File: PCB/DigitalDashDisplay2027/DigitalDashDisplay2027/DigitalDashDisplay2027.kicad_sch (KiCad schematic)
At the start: 13 parts, among them IC1 LMR51430YDDCR, J1 Adafruit CAN Pal, J2 53375-0810, U1 Teensy4.0

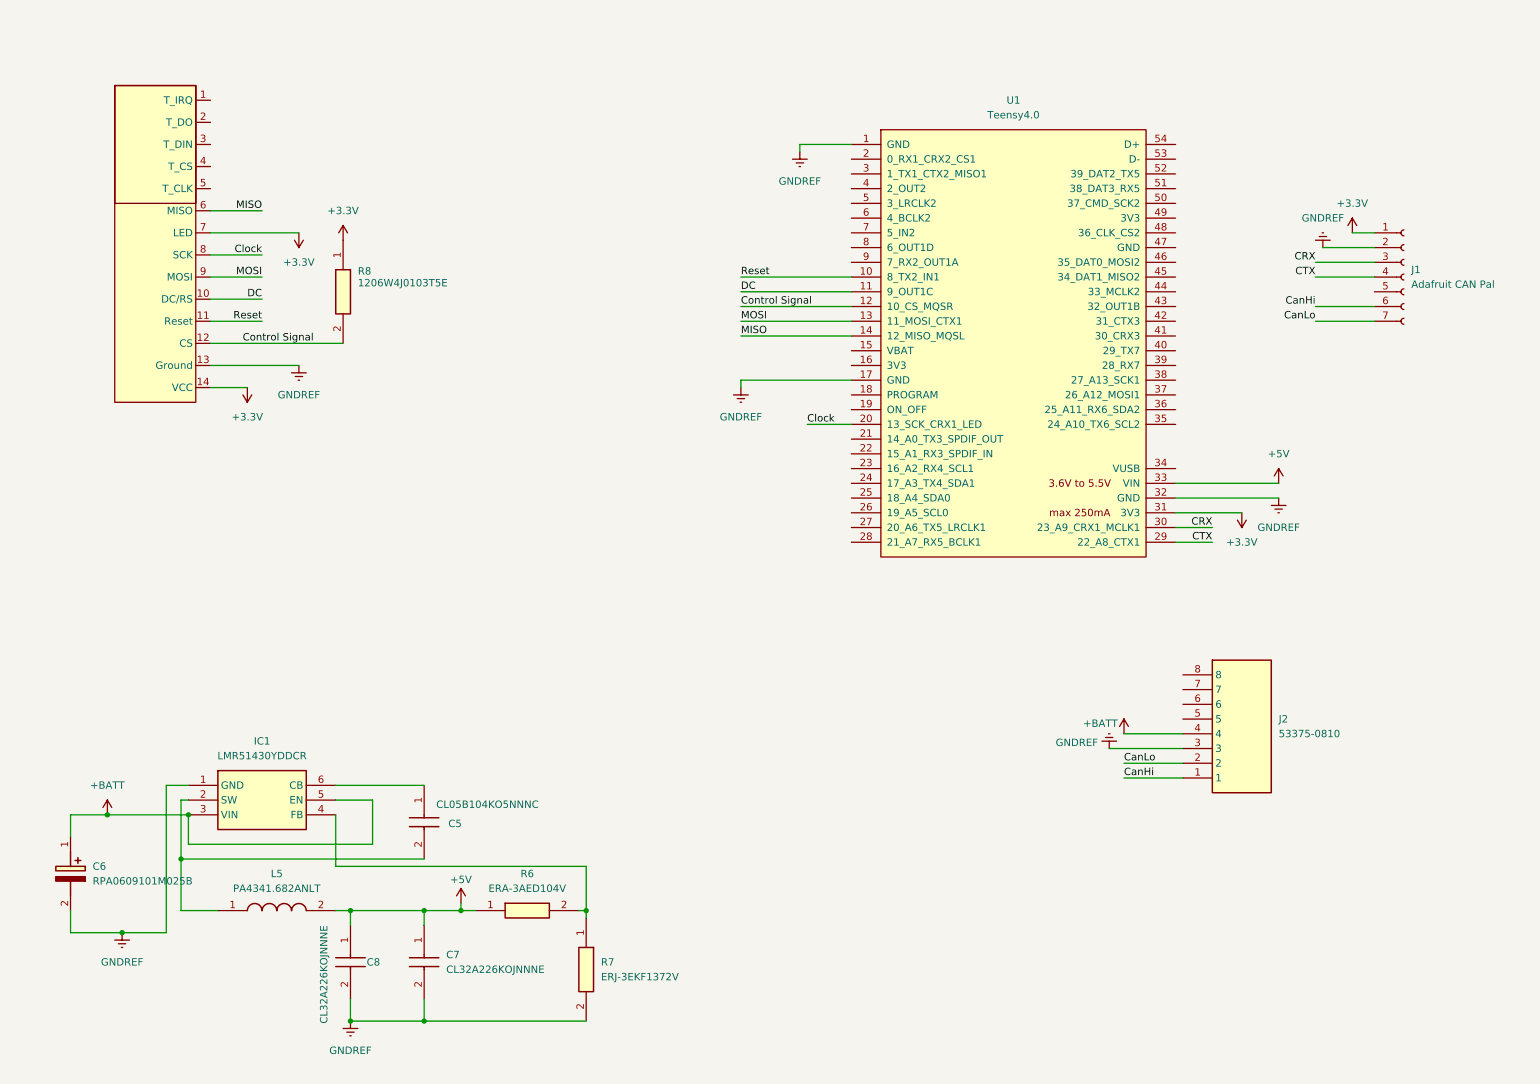
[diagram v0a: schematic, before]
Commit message: Began restructuring dash PCB, migrated footprints & symbols to the central library
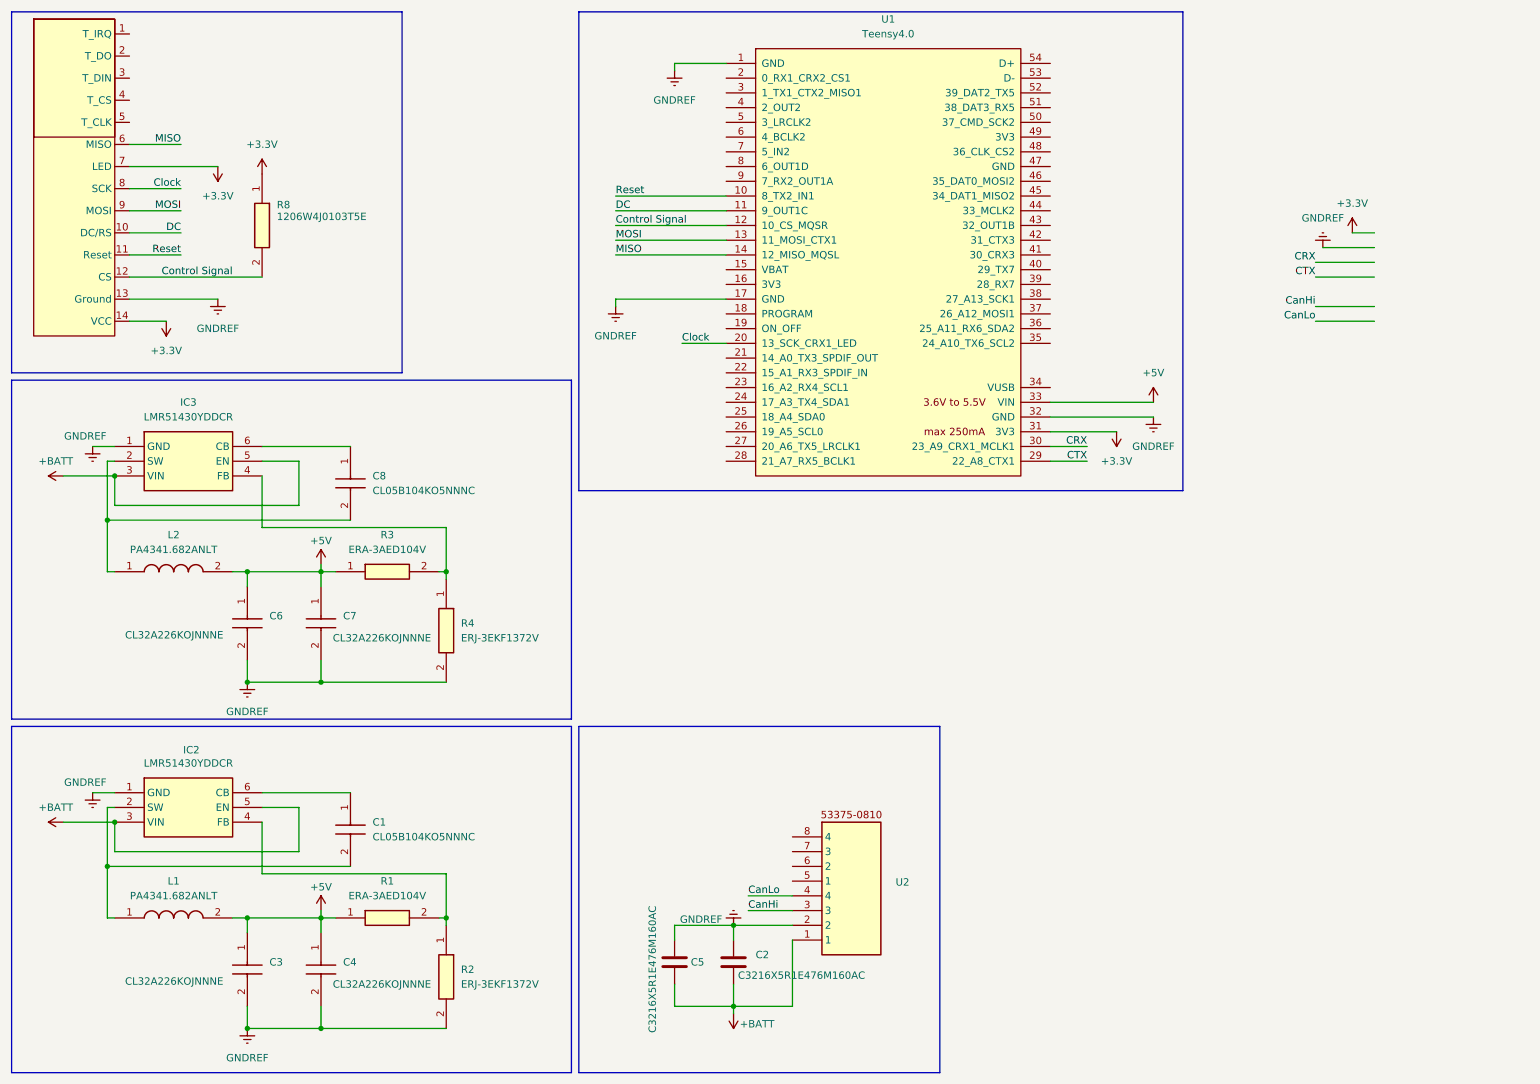
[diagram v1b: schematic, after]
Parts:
- removed C5: CL05B104KO5NNNC, buck_footprints:CAPC1005X55N, symbol CL05B104KO5NNNC:CL05B104KO5NNNC
- removed C6: RPA0609101M025B, buck_footprints:CAPPRD250W55D630H1050, symbol RPA0609101M025B:RPA0609101M025B
- removed C7, C8: CL32A226KOJNNNE, buck_footprints:CAPC3225X270N, symbol CL32A226KOJNNNE:CL32A226KOJNNNE
- removed IC1: LMR51430YDDCR, buck_footprints:SOT95P280X110-6N, symbol LMR51430YDDCR:LMR51430YDDCR
- removed J1: Adafruit CAN Pal, CFR 2025 Digital Dash Lib:1X07_ROUND_70, symbol Connector:Conn_01x07_Socket
- removed J2: 53375-0810, 533750810, symbol SamacSys_Parts:53375-0810
- removed L5: PA4341.682ANLT, buck_footprints:INDPM7166X300N, symbol PA4341_682ANLT:PA4341.682ANLT
- removed R6: ERA-3AED104V, buck_footprints:ERA3AEB101V, symbol ERA-3AED104V:ERA-3AED104V
- removed R7: ERJ-3EKF1372V, buck_footprints:RESC1608X55N, symbol ERJ-3EKF1372V:ERJ-3EKF1372V
- added C1, C8: CL05B104KO5NNNC, CAPC1005X55N, symbol CFR Library:CL05B104KO5NNNC
- added C2, C5: C3216X5R1E476M160AC, Capacitor_SMD:C_1206_3216Metric_Pad1.33x1.80mm_HandSolder, symbol Device:C
- added C3, C4, C6, C7: CL32A226KOJNNNE, CAPC3225X270N, symbol CFR Library:CL32A226KOJNNNE
- added IC2, IC3: LMR51430YDDCR, SOT95P280X110-6N, symbol CFR Library:LMR51430YDDCR
- added L1, L2: PA4341.682ANLT, INDPM7166X300N, symbol CFR Library:PA4341.682ANLT
- added R1, R3: ERA-3AED104V, ERA3AEB101V, symbol CFR Library:ERA-3AED104V
- added R2, R4: ERJ-3EKF1372V, RESC1608X55N, symbol CFR Library:ERJ-3EKF1372V
- added U2: (no value), CFR-Footprint-Library:CONN08_533750810_MOL, symbol CFR Library:53375-0810
- ILI1: value ~ -> (none)
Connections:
- net +5V: now also C3.1, C4.1, C6.1, C7.1, L1.2, L2.2, R1.1, R3.1
- net +BATT: now also C2.2, C5.2, IC2.3 (VIN), IC2.5 (EN), IC3.3 (VIN), IC3.5 (EN), U2.1
- net CanHi: now also U2.3
- net CanLo: now also U2.4
- net GNDREF: now also C2.1, C3.2, C4.2, C5.1, C6.2, C7.2, IC2.1 (GND), IC3.1 (GND), R2.2, R4.2, U2.2
- new net: C8.2, IC3.2 (SW), L2.1
- new net: C1.2, IC2.2 (SW), L1.1
- new net: IC2.4 (FB), R1.2, R2.1
- new net: IC3.4 (FB), R3.2, R4.1
- new net: C1.1, IC2.6 (CB)
- new net: C8.1, IC3.6 (CB)
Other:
- moved on the sheet: R8, U1

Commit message: Began redesigning dashboard, changed multi-power rail to single power rail, rerouted buck converter
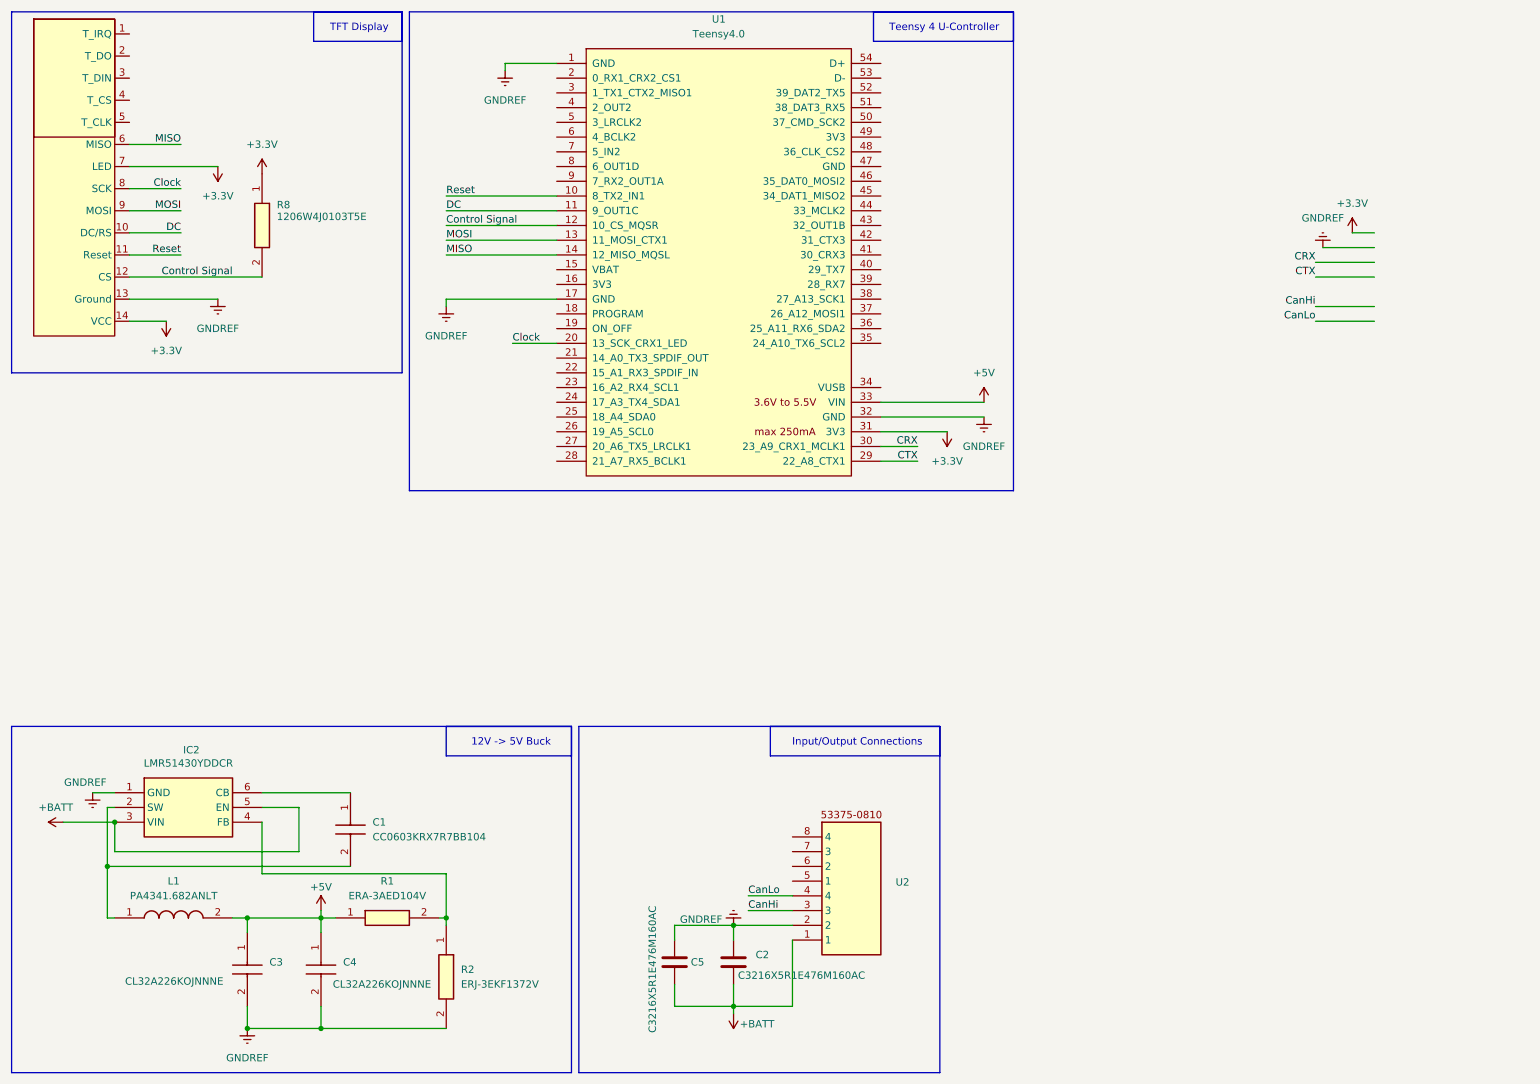
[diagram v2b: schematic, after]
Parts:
- removed C6, C7: CL32A226KOJNNNE, CAPC3225X270N, symbol CFR Library:CL32A226KOJNNNE
- removed C8: CL05B104KO5NNNC, CAPC1005X55N, symbol CFR Library:CL05B104KO5NNNC
- removed IC3: LMR51430YDDCR, SOT95P280X110-6N, symbol CFR Library:LMR51430YDDCR
- removed L2: PA4341.682ANLT, INDPM7166X300N, symbol CFR Library:PA4341.682ANLT
- removed R3: ERA-3AED104V, ERA3AEB101V, symbol CFR Library:ERA-3AED104V
- removed R4: ERJ-3EKF1372V, RESC1608X55N, symbol CFR Library:ERJ-3EKF1372V
- C1: value CL05B104KO5NNNC -> CC0603KRX7R7BB104; footprint CAPC1005X55N -> Capacitor_SMD:C_0603_1608Metric
- C3, C4: footprint CAPC3225X270N -> Capacitor_SMD:C_1210_3225Metric
- IC2: footprint SOT95P280X110-6N -> CFR Library:SOT95P280X110-6N
- L1: footprint INDPM7166X300N -> CFR Library:INDPM7166X300N
- R1: footprint ERA3AEB101V -> Resistor_SMD:R_0603_1608Metric
- R2: footprint RESC1608X55N -> Resistor_SMD:R_0603_1608Metric
- U2: footprint CFR-Footprint-Library:CONN08_533750810_MOL -> CFR Library:CONN08_533750810_MOL
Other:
- note added: "12V -> 5V Buck"
- note added: "Input/Output Connections"
- note added: "TFT Display"
- note added: "Teensy 4 U-Controller"
- moved on the sheet: U1

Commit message: V1.0 of dashboard, plus minor changes to DAQ board
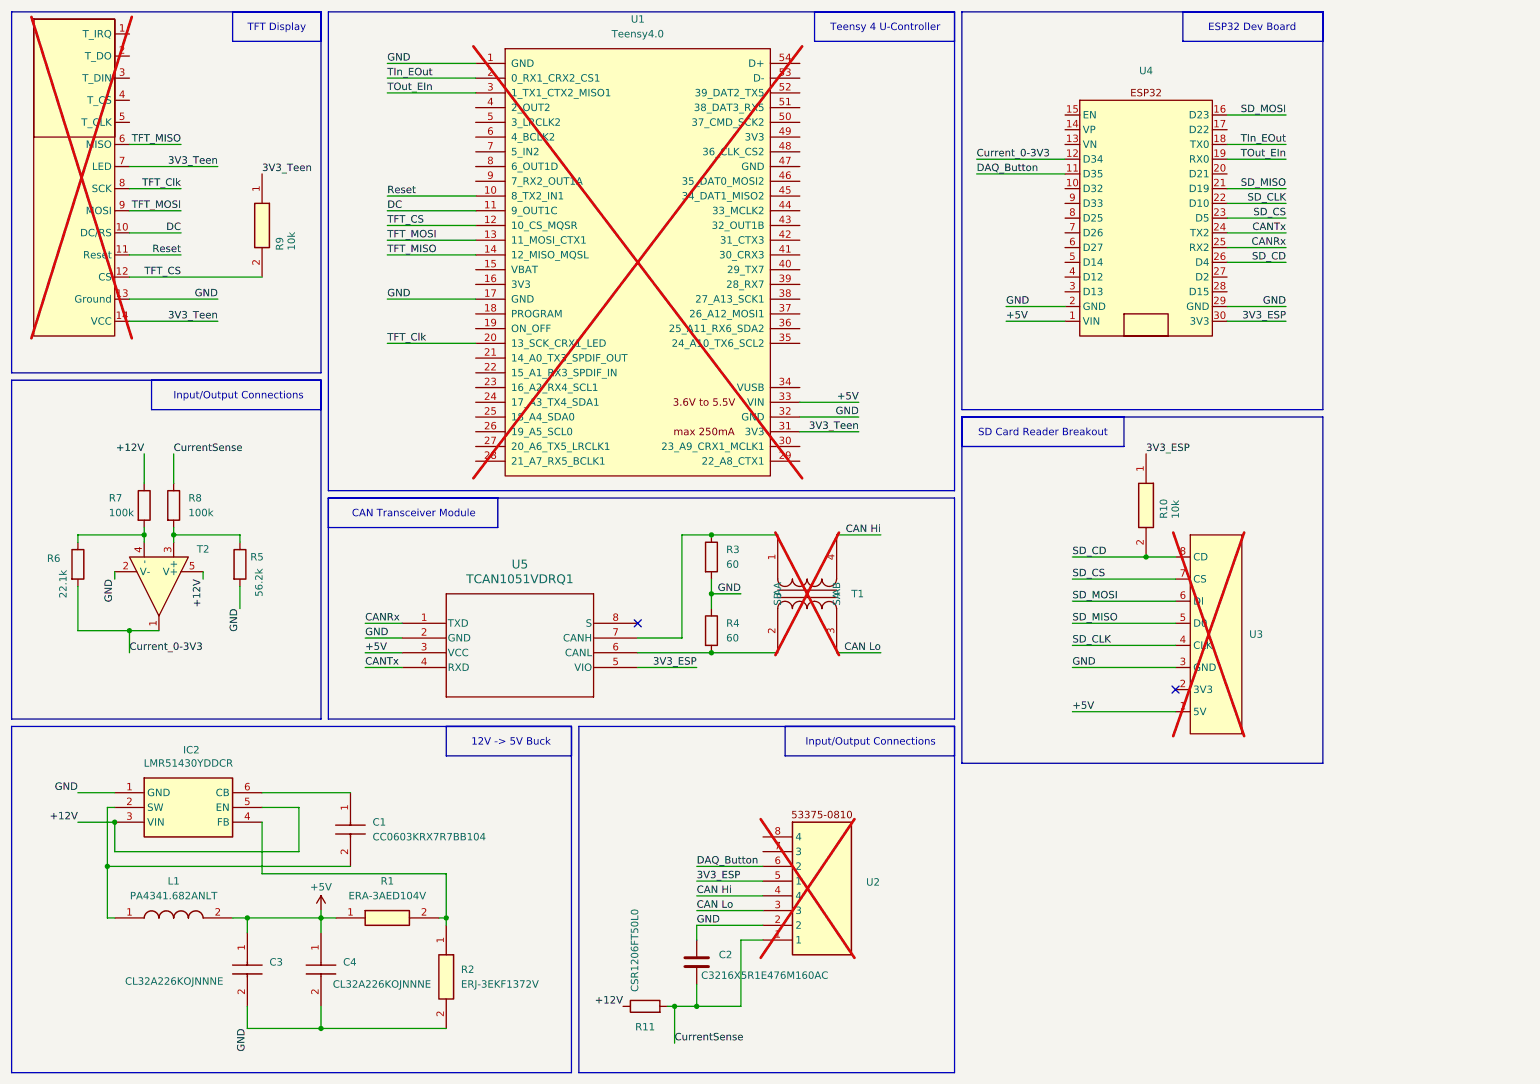
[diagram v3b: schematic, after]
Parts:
- removed C5: C3216X5R1E476M160AC, Capacitor_SMD:C_1206_3216Metric_Pad1.33x1.80mm_HandSolder, symbol Device:C
- added R10: 10k, Resistor_SMD:R_0603_1608Metric_Pad0.98x0.95mm_HandSolder, symbol 1206W4J0103T5E:1206W4J0103T5E
- added R11: CSR1206FT50L0, Resistor_SMD:R_1206_3216Metric, symbol Device:R
- added R3, R4: 60, Resistor_SMD:R_0603_1608Metric, symbol Device:R
- added R5: 56.2k, Resistor_SMD:R_0402_1005Metric, symbol Device:R
- added R6: 22.1k, Resistor_SMD:R_0402_1005Metric, symbol Device:R
- added R7, R8: 100k, Resistor_SMD:R_0402_1005Metric, symbol Device:R
- added T1: (no value), CFR-Footprint-Library:AC1210-110-C, symbol CFR Library:AC1210-110-C
- added T2: (no value), CFR-Footprint-Library:NCS2005SN1T1G, symbol CFR Library:NCS2005SN1T1G
- added U3: (no value), CFR-Footprint-Library:Adafruit 254, symbol CFR Library:Adafruit_254
- added U4: (no value), CFR-Footprint-Library:ESP32, symbol CFR Library:ESP32
- added U5: TCAN1051VDRQ1, CFR-Footprint-Library:D8_TEX, symbol CFR-Symbol-Library:TCAN1051VDRQ1
- ILI1, U1, U2: now not fitted
- R9: renamed from R8; value 1206W4J0103T5E -> 10k; footprint RESC3116X65N -> Resistor_SMD:R_0603_1608Metric_Pad0.98x0.95mm_HandSolder; Height 0.65 -> (none); Manufacturer_Name UNI-ROYAL(Uniroyal Elec) -> Yageo; Manufacturer_Part_Number 1206W4J0103T5E -> RC0603JR-0710KL
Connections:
- net +5V: now also U3.1 (5V), U4.1 (VIN), U5.3 (VCC)
- net 3V3_ESP: now reaches U2.5 (1)
- net 3V3_ESP: now also R10.1, U4.30 (3V3), U5.5 (VIO)
- net DAQ_Button: now reaches U2.6 (2)
- net DAQ_Button: now also U4.11 (D35)
- net TIn_EOut: now reaches U1.2 (0_RX1_CRX2_CS1)
- net TIn_EOut: now also U4.18 (TX0)
- net TOut_EIn: now reaches U1.3 (1_TX1_CTX2_MISO1)
- net TOut_EIn: now also U4.19 (RX0)
- net +3.3V renamed 3V3_Teen
- net +BATT renamed +12V
- net +12V: now also R11.1, R7.1, T2.5 (V+); no longer C2.2, U2.1
- net CRX: no longer names the net of U1.30 (23_A9_CRX1_MCLK1)
- net CTX: no longer names the net of U1.29 (22_A8_CTX1)
- net CanHi renamed CAN Lo
- net CAN Lo: now also T1.3 (SA)
- net CanLo renamed CAN Hi
- net CAN Hi: now also T1.4 (AB)
- net Clock renamed TFT_Clk
- net Control Signal renamed TFT_CS
- net GNDREF renamed GND
- net GND: now also R3.2, R4.1, R5.2, T2.2 (V-), U3.3 (GND), U4.2 (GND), U4.29 (GND), U5.2 (GND)
- net MISO renamed TFT_MISO
- net MOSI renamed TFT_MOSI
- new net: R6.1, R7.2, T2.4 (-)
- new net: R4.2, T1.2 (SB), U5.6 (CANL)
- new net: R5.1, R8.2, T2.3 (+)
- new net: R3.1, T1.1 (AA), U5.7 (CANH)
- new net CANRx: U4.25 (RX2), U5.1 (TXD)
- new net CANTx: U4.24 (TX2), U5.4 (RXD)
- new net CurrentSense: C2.2, R11.2, R8.1, U2.1
- new net Current_0-3V3: R6.2, T2.1, U4.12 (D34)
- new net SD_CD: R10.2, U3.8 (CD), U4.26 (D4)
- new net SD_CLK: U3.4 (CLK), U4.22 (D10)
- new net SD_CS: U3.7 (CS), U4.23 (D5)
- new net SD_MISO: U3.5 (D0), U4.21 (D19)
- new net SD_MOSI: U3.6 (DI), U4.16 (D23)
- no-connect marks 0 -> 2
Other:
- note added: "CAN Transceiver Module"
- note added: "ESP32 Dev Board"
- note added: "SD Card Reader Breakout"
- title: CFR Digital Dashboard 2025 -> CFR Digital Dashboard 2027
- moved on the sheet: C2
